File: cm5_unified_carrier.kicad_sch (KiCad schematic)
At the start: 13 parts, among them J101 436500403, J102 484050003, J103 484050003

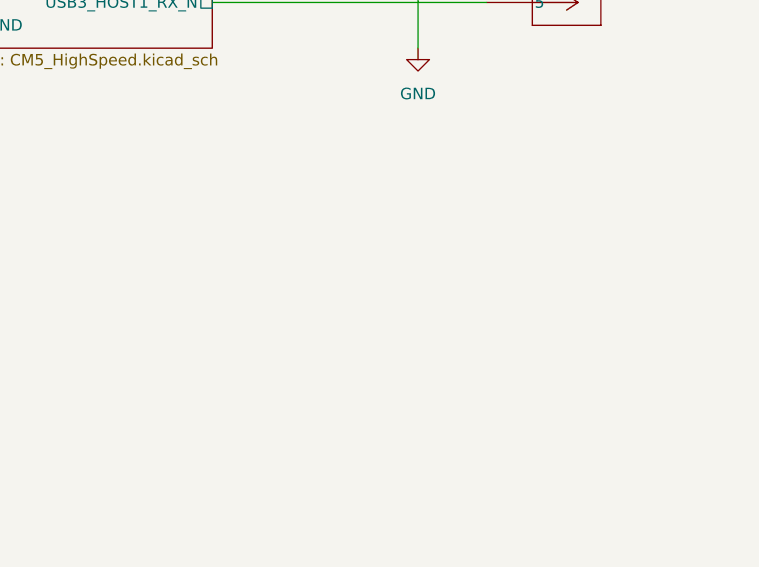
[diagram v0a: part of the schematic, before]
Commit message: Added another barrel jack for 12V output for ASI camera
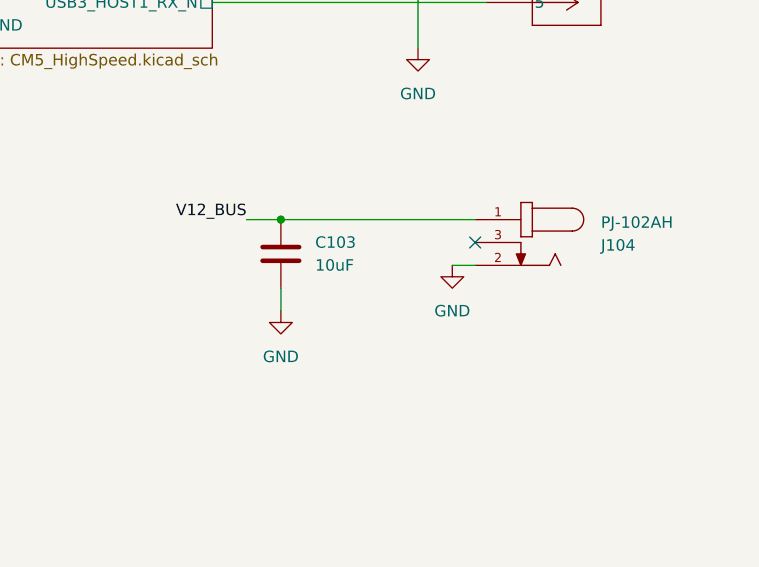
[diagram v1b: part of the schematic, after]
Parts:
- added C103: 10uF, Capacitor_SMD:C_1206_3216Metric_Pad1.33x1.80mm_HandSolder, symbol Device:C
- added J104: PJ-102AH, PJ-102AH:CUI_PJ-102AH, symbol PJ-102AH:PJ-102AH
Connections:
- net GND: now also C103.2, J104.2
- net V12_BUS: now also C103.1, J104.1
- no-connect marks 5 -> 6

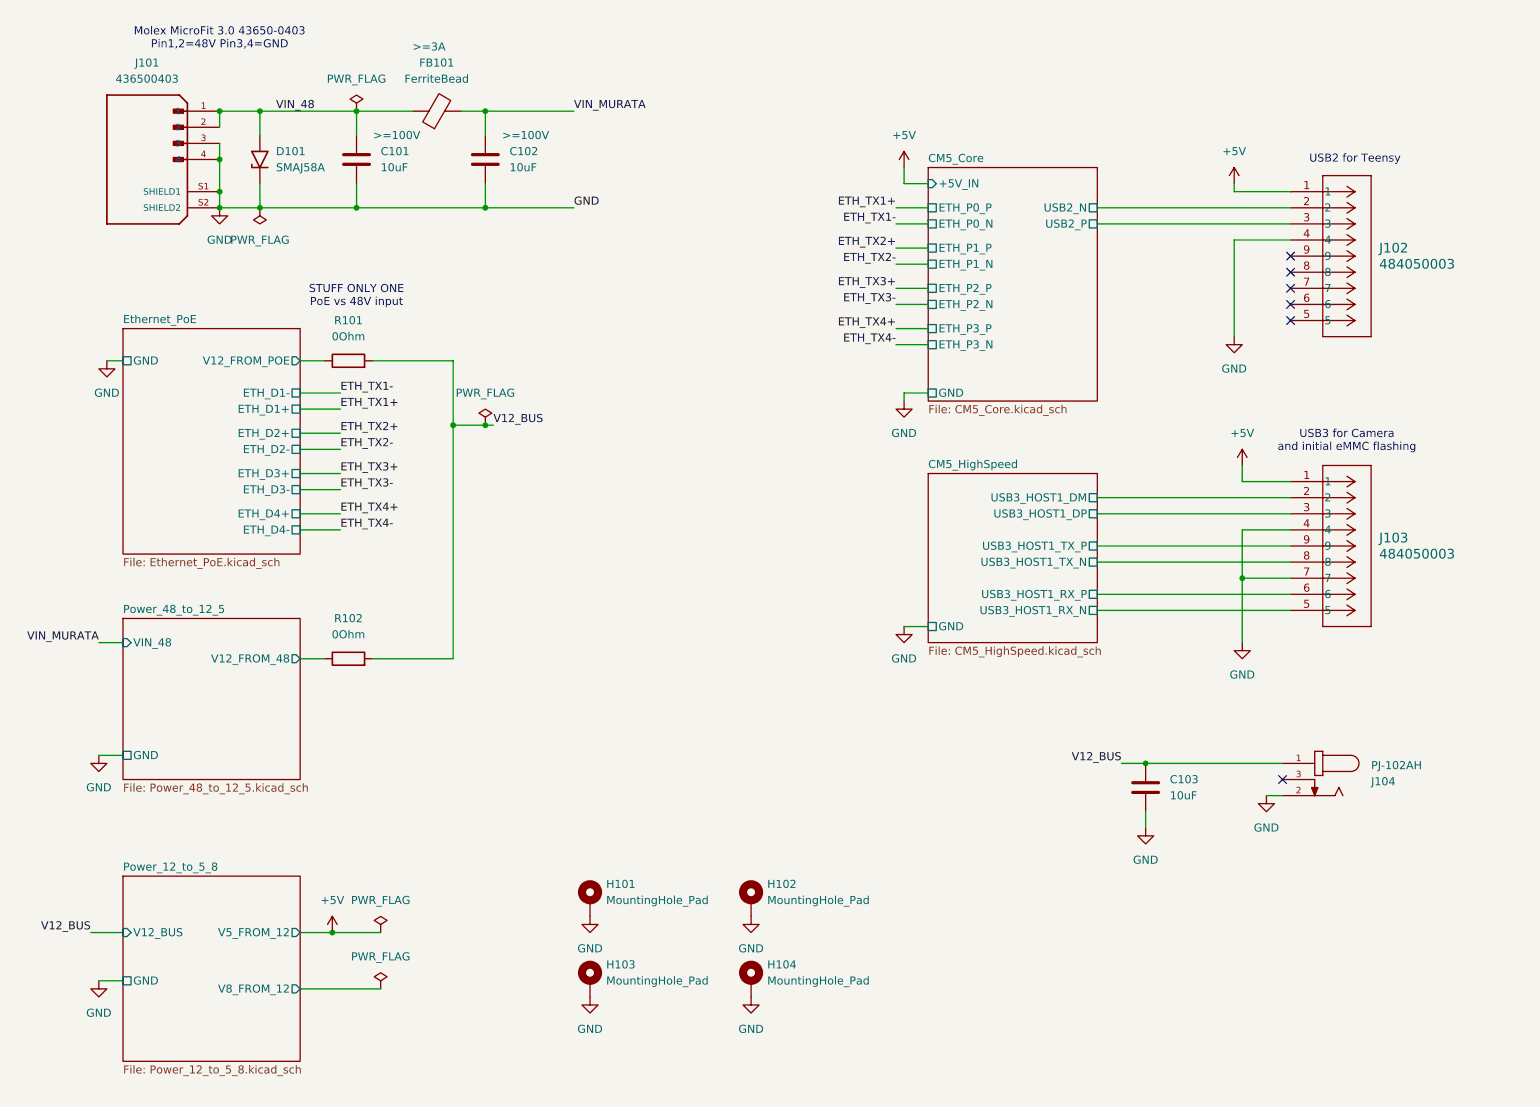
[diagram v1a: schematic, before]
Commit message: Added USB connector for flashing eMMC and related switches
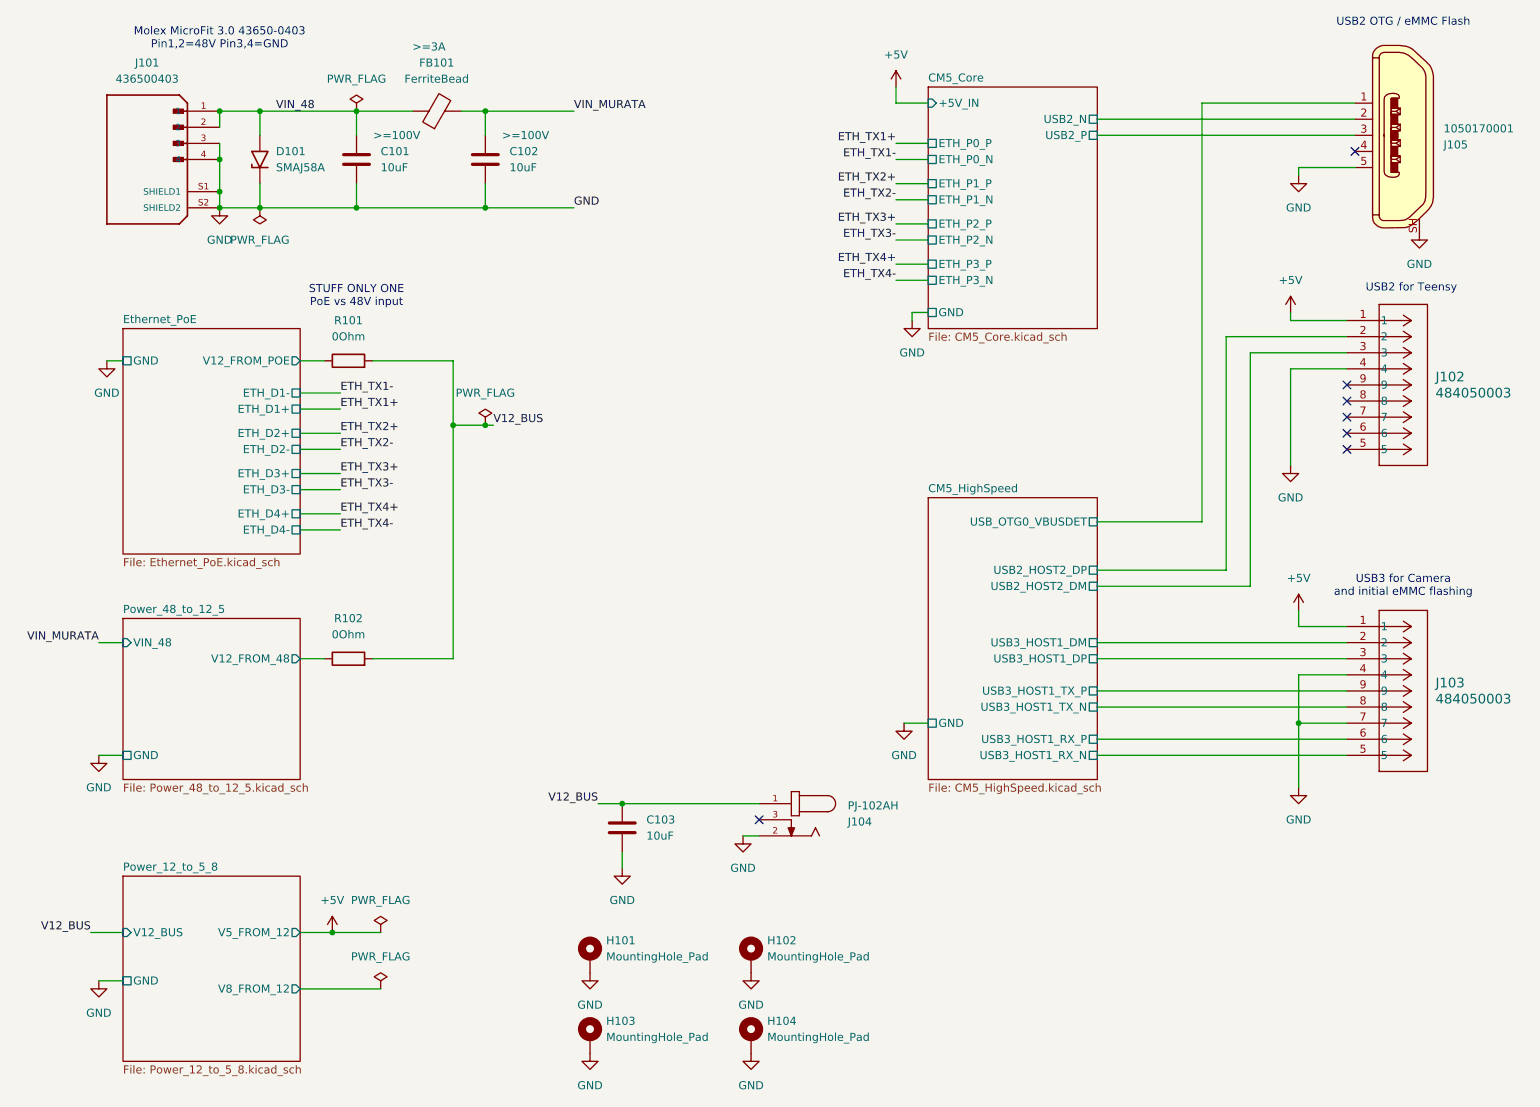
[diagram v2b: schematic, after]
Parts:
- added J105: 1050170001, digikey-footprints:USB_Micro_B_Female_1050170001, symbol dk_USB-DVI-HDMI-Connectors:1050170001
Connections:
- net CM5_Core/USB2_N: now also J105.2; no longer J102.2
- net CM5_Core/USB2_P: now also J105.3; no longer J102.3
- net GND: now also J105.5, J105.SH
- new net CM5_HighSpeed/USB2_HOST2_DM: J102.3
- new net CM5_HighSpeed/USB2_HOST2_DP: J102.2
- new net CM5_HighSpeed/USB_OTG0_VBUSDET: J105.1
- no-connect marks 6 -> 7
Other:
- sheet CM5_HighSpeed ports: added USB2_HOST2_DM, USB2_HOST2_DP, USB_OTG0_VBUSDET; removed none
- note added: "USB2 OTG / eMMC Flash"
- moved on the sheet: C103, H101, H102, H103, H104, J102, J103, J104
